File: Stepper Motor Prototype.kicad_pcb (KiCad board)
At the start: 2 copper layers, 142 x 61 mm, 64 parts, among them J1 USB_B_Micro, J2 Screw_Terminal_01x02, J3 Screw_Terminal_01x04, Q1 STD20NF06L, Q2 STD20NF06L, Q3 STD20NF06L, Q4 STD20NF06L, Q5 STD20NF06L, Q6 STD20NF06L, Q7 STD20NF06L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

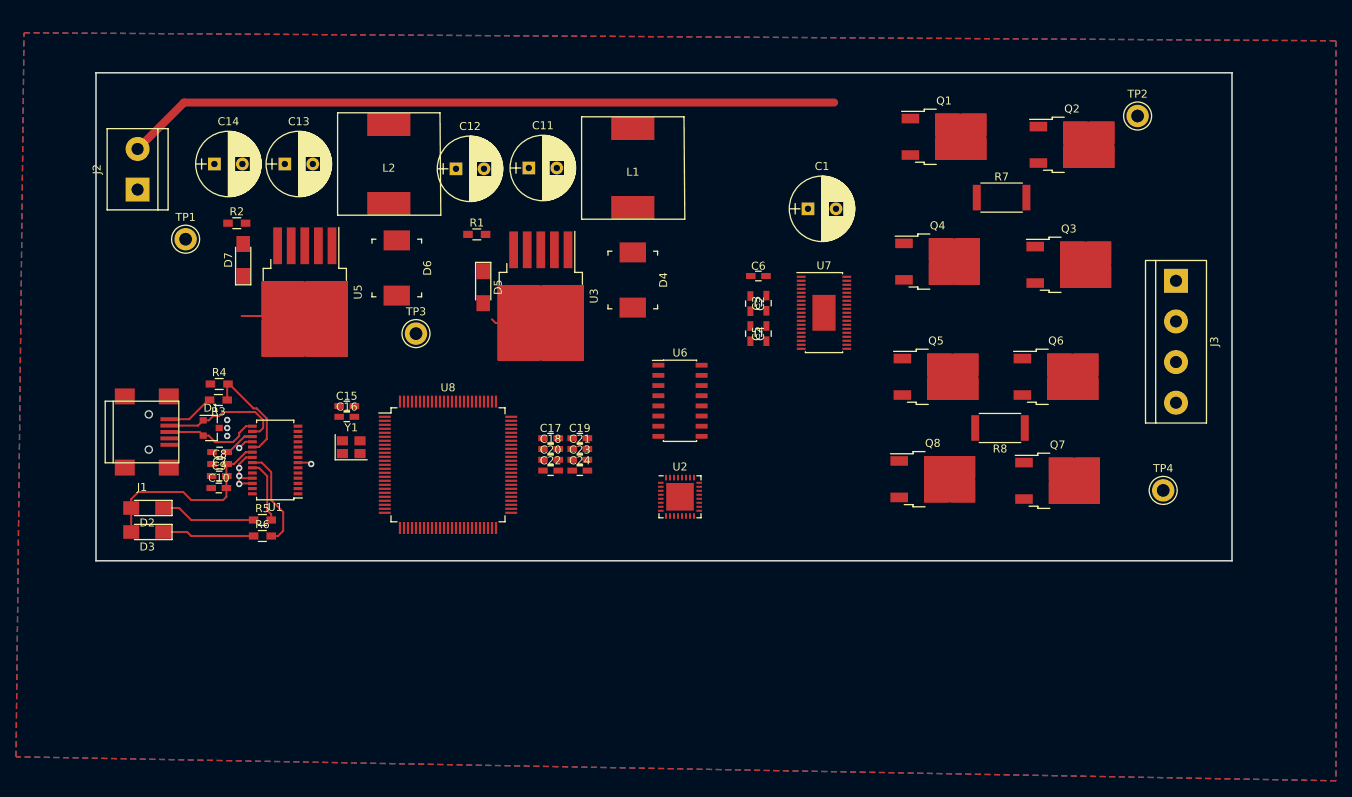
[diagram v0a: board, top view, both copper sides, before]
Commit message: added logic level shifters
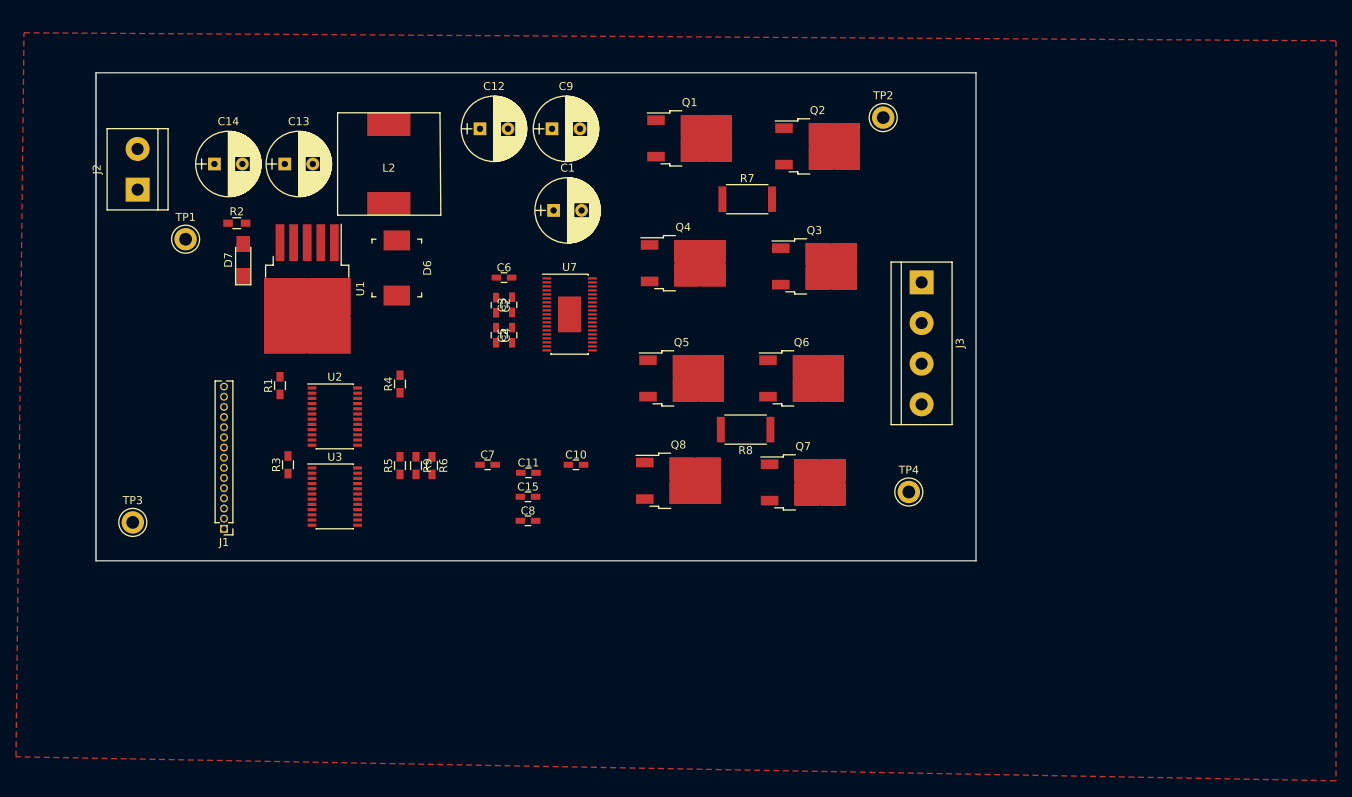
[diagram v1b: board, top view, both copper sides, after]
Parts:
- removed C16: C, Capacitors_SMD:C_0603_HandSoldering
- removed C17, C18, C19, C20, C21, C22, C23, C24: 0.1uF, Capacitors_SMD:C_0603_HandSoldering
- removed D1: SP0502BAHT, TO_SOT_Packages_SMD:SOT-23
- removed D2: TX_LED, LEDs:LED_1206_HandSoldering
- removed D3: RX_LED, LEDs:LED_1206_HandSoldering
- removed D4: D_Schottky, digikey-footprints:DO-214AB
- removed D5: LED, LEDs:LED_1206_HandSoldering
- removed L1: 100uH, my_inductors:Wurth_SMD_Inductor_7447709101
- removed U5: LM2595SX-5.0_NOPB, TO_SOT_Packages_SMD:TO-263-5_TabPin3
- removed U6: S25FL512SAGMFIG11, Housings_SOIC:SOIC-16_3.9x9.9mm_Pitch1.27mm
- removed U8: STM32F407VGTx, Housings_QFP:LQFP-100_14x14mm_Pitch0.5mm
- removed Y1: Crystal_GND24, Crystals:Crystal_SMD_SeikoEpson_TSX3225-4pin_3.2x2.5mm
- added R9: 10k, Resistors_SMD:R_0603_HandSoldering, F.Cu at (110.0, 106.1)
- C10: value 4.7uF -> 0.1uF
- C11: value 120uF -> 0.1uF; footprint Capacitors_THT:CP_Radial_D8.0mm_P3.50mm -> Capacitors_SMD:C_0603_HandSoldering
- C12: value 150uF -> 100uF
- C15: value C -> 1uF
- C9: value 0.1uF -> 100uF; footprint Capacitors_SMD:C_0603_HandSoldering -> Capacitors_THT:CP_Radial_D8.0mm_P3.50mm
- J1: value USB_B_Micro -> Conn_01x15; footprint Connectors:USB_Mini-B -> Pin_Headers:Pin_Header_Straight_1x15_Pitch1.27mm
- R1, R5, R6: value 330R -> 10k
- R3: value 4k7 -> 10k
- U1: value FT232RL -> LM2595SX-5.0_NOPB; footprint Housings_SSOP:TSSOP-28_4.4x9.7mm_Pitch0.65mm -> TO_SOT_Packages_SMD:TO-263-5_TabPin3
- U2: value ESP8266EX -> SN74AXC8T245; footprint Housings_DFN_QFN:QFN-32-1EP_5x5mm_Pitch0.5mm -> Housings_SSOP:TSSOP-24_4.4x7.8mm_Pitch0.65mm
- U3: value LM2595SX-3.3_NOPB -> SN74AXC8T245; footprint TO_SOT_Packages_SMD:TO-263-5_TabPin3 -> Housings_SSOP:TSSOP-24_4.4x7.8mm_Pitch0.65mm
- moved C9 60.1 mm to (127.0, 64.0)
- moved C10 44.7 mm to (130.0, 106.0)
- moved U2 44.3 mm to (99.8, 100.0)
- moved TP3 42.5 mm to (74.6, 113.2)
- moved C8 39.2 mm to (124.0, 113.0)
- moved C11 38.1 mm to (124.0, 107.0)
- moved U3 35.9 mm to (99.8, 110.0), turned to 0 degrees
- moved C7 33.5 mm to (119.0, 106.0), turned to 0 degrees
- moved C2 31.8 mm to (120.0, 86.0)
- moved C3 31.8 mm to (122.0, 86.0)
- moved C4 31.8 mm to (120.0, 89.8)
- moved C5 31.8 mm to (122.0, 89.8)
- moved C6 31.8 mm to (121.0, 82.6)
- moved J3 31.8 mm to (173.2, 83.2)
- moved Q1 31.8 mm to (144.2, 65.2)
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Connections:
- C10 pad 2: +5V -> +1V8
- C11 pad 2: +24V -> +1V8
- C12 pad 1: GND -> +24V
- C12 pad 2: +3V3 -> GND
- C7 pad 1: Net-(C7-Pad1) -> GND
- C7 pad 2: GND -> +3V3
- C8 pad 2: +5V -> +3V3
- C9 pad 1: GND -> +24V
- C9 pad 2: +5V -> GND
- J1 pad 1: Net-(J1-Pad1) -> GND
- J1 pad 2: Net-(D1-Pad1) -> +5V
- J1 pad 3: Net-(D1-Pad2) -> Net-(J1-Pad3)
- J1 pad 4: (no net) -> Net-(J1-Pad4)
- J1 pad 5: GND -> Net-(J1-Pad5)
- J1 pad 6: GND -> Net-(J1-Pad6)
- R1 pad 1: Net-(D5-Pad2) -> Net-(R1-Pad1)
- R3 pad 2: Net-(J1-Pad1) -> +3V3
- R4 pad 1: GND -> Net-(R4-Pad1)
- R4 pad 2: Net-(R3-Pad1) -> +3V3
- R5 pad 1: Net-(D2-Pad1) -> Net-(R5-Pad1)
- R5 pad 2: Net-(R5-Pad2) -> +3V3
- R6 pad 1: Net-(D3-Pad1) -> +1V8
- U1 pad 1: (no net) -> Net-(D6-Pad1)
- U1 pad 2: (no net) -> +24V
- U1 pad 3: (no net) -> GND
- U1 pad 4: Net-(C7-Pad1) -> +5V
- U1 pad 5: (no net) -> GND
- U2 pad 1: (no net) -> +3V3
- U2 pad 11: (no net) -> GND
- U2 pad 12: (no net) -> GND
- U2 pad 13: (no net) -> GND
- U2 pad 16: (no net) -> Net-(U2-Pad16)
- U2 pad 17: (no net) -> Net-(U2-Pad17)
- U2 pad 18: (no net) -> Net-(U2-Pad18)
- U2 pad 19: (no net) -> Net-(U2-Pad19)
- U2 pad 2: (no net) -> Net-(R1-Pad1)
- U2 pad 20: (no net) -> Net-(U2-Pad20)
- U2 pad 21: (no net) -> Net-(U2-Pad21)
- U2 pad 22: (no net) -> Net-(R4-Pad1)
- U2 pad 23: (no net) -> +1V8
- U2 pad 24: (no net) -> +1V8
- U2 pad 3: (no net) -> Net-(J1-Pad15)
- U2 pad 4: (no net) -> Net-(J1-Pad14)
- U2 pad 5: (no net) -> Net-(J1-Pad13)
- U2 pad 6: (no net) -> Net-(J1-Pad12)
- U2 pad 7: (no net) -> Net-(J1-Pad11)
- U2 pad 8: (no net) -> Net-(J1-Pad10)
- U3 pad 1: Net-(D4-Pad1) -> +3V3
- U3 pad 2: +24V -> Net-(R3-Pad1)
- U3 pad 3: GND -> Net-(J1-Pad9)
- U3 pad 4: +3V3 -> Net-(J1-Pad8)
- U3 pad 5: GND -> Net-(J1-Pad7)
- U7 pad 10: (no net) -> Net-(U2-Pad19)
- U7 pad 11: (no net) -> Net-(U2-Pad18)
- U7 pad 12: (no net) -> Net-(U2-Pad17)
- U7 pad 13: (no net) -> Net-(U2-Pad16)
- U7 pad 14: (no net) -> Net-(U3-Pad21)
- U7 pad 15: (no net) -> Net-(U3-Pad20)
- U7 pad 16: (no net) -> Net-(U3-Pad19)
- U7 pad 17: (no net) -> Net-(U3-Pad18)
- U7 pad 18: (no net) -> Net-(R9-Pad2)
- U7 pad 19: (no net) -> Net-(R6-Pad2)
- U7 pad 20: (no net) -> Net-(C15-Pad1)
- U7 pad 8: (no net) -> Net-(U2-Pad21)
- U7 pad 9: (no net) -> Net-(U2-Pad20)
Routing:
- net +24V: track 89.5 -> 0.00 mm
- net GND: track 29.8 -> 0.00 mm, vias 8 -> 0
- net +5V: track 24.9 -> 0.00 mm
- net Net-(D1-Pad1): track 15.3 -> 0.00 mm
- net Net-(R3-Pad1): track 13.5 -> 0.00 mm
- net Net-(R6-Pad2): track 12.6 -> 0.00 mm
- net Net-(D2-Pad1): track 11.9 -> 0.00 mm
- net Net-(D1-Pad2): track 11.9 -> 0.00 mm
- net Net-(D3-Pad1): track 11.5 -> 0.00 mm
- net Net-(R5-Pad2): track 7.98 -> 0.00 mm
- net Net-(J1-Pad1): track 5.99 -> 0.00 mm
- net Net-(C7-Pad1): track 4.35 -> 0.00 mm
- removed copper zone on B.Cu, net GND
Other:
- board size 142 x 61 mm -> 110 x 61 mm

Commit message: removed power supply, basic layout of 1 motor winding complete
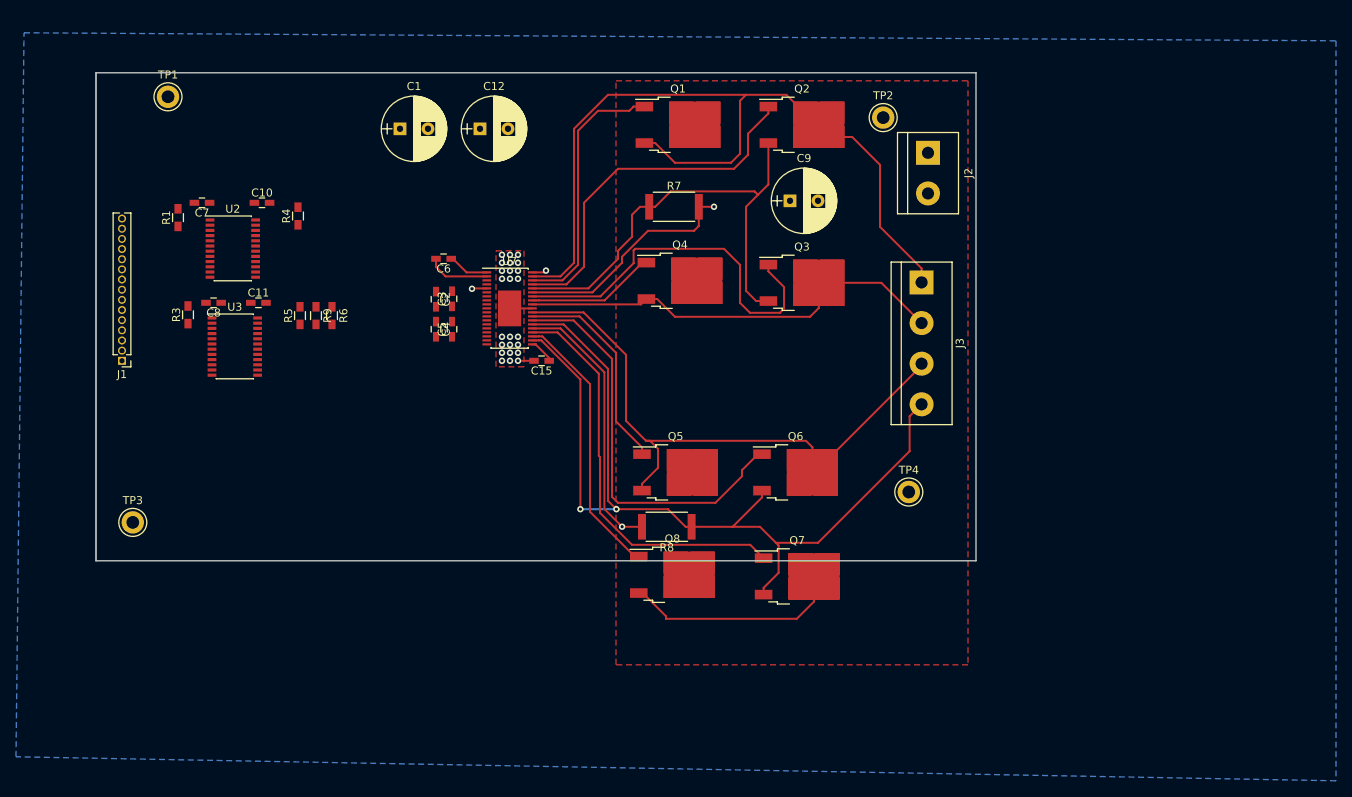
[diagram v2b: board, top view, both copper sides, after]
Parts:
- removed C13: 120uF, Capacitors_THT:CP_Radial_D8.0mm_P3.50mm
- removed C14: 150uF, Capacitors_THT:CP_Radial_D8.0mm_P3.50mm
- removed D6: D_Schottky, digikey-footprints:DO-214AB
- removed D7: LED, LEDs:LED_1206_HandSoldering
- removed L2: L, my_inductors:Wurth_SMD_Inductor_7447709101
- removed R2: 330R, Resistors_SMD:R_0603_HandSoldering
- removed U1: LM2595SX-5.0_NOPB, TO_SOT_Packages_SMD:TO-263-5_TabPin3
- J1: value Conn_01x15 -> Conn_01x16
- moved J2 98.9 mm to (174.0, 67.0), turned to 270 degrees
- moved C10 51.1 mm to (90.8, 73.2)
- moved C7 48.4 mm to (83.2, 73.2), turned to 180 degrees
- moved C8 47.8 mm to (84.7, 85.8), turned to 180 degrees
- moved C11 39.9 mm to (90.3, 85.8)
- moved C9 31.1 mm to (156.8, 73.0)
- moved J1 24.6 mm to (73.2, 93.0)
- moved R1 24.6 mm to (80.2, 75.1)
- moved R4 24.6 mm to (95.2, 74.9)
- moved U2 24.6 mm to (87.1, 79.0)
- moved R3 22.5 mm to (81.5, 87.2)
- moved R5 22.5 mm to (95.5, 87.3)
- moved R6 22.5 mm to (99.5, 87.3)
- moved R9 22.5 mm to (97.5, 87.3)
- moved U3 22.5 mm to (87.3, 91.2)
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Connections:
- net Net-(J3-Pad1) renamed /AOUT1
- net Net-(J3-Pad2) renamed /AOUT2
- net Net-(Q1-Pad1) renamed /A1HS
- net Net-(Q2-Pad1) renamed /A1LS
- net Net-(Q2-Pad3) renamed /A1SENP
- net Net-(Q3-Pad1) renamed /A2LS
- net Net-(Q4-Pad1) renamed /A2HS
- J1 pad 2: +5V -> +1V8
- J1 pad 3: Net-(J1-Pad3) -> +3V3
- U2 pad 3: Net-(J1-Pad15) -> (no net)
- U2 pad 4: Net-(J1-Pad14) -> Net-(J1-Pad15)
- U2 pad 5: Net-(J1-Pad13) -> Net-(J1-Pad14)
- U2 pad 6: Net-(J1-Pad12) -> Net-(J1-Pad13)
- U2 pad 7: Net-(J1-Pad11) -> Net-(J1-Pad12)
- U2 pad 8: Net-(J1-Pad10) -> Net-(J1-Pad11)
- U3 pad 3: Net-(J1-Pad9) -> Net-(J1-Pad10)
- U3 pad 4: Net-(J1-Pad8) -> Net-(J1-Pad9)
- U3 pad 5: Net-(J1-Pad7) -> Net-(J1-Pad8)
- U3 pad 6: Net-(J1-Pad6) -> Net-(J1-Pad7)
- U3 pad 7: Net-(J1-Pad5) -> Net-(J1-Pad6)
- U3 pad 8: Net-(J1-Pad4) -> Net-(J1-Pad5)
- U3 pad 9: Net-(J1-Pad3) -> Net-(J1-Pad4)
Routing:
- net Net-(J3-Pad4): track 0.00 -> 121.5 mm, vias 0 -> 2
- net /AOUT1: track 0.00 -> 102.0 mm
- net Net-(J3-Pad3): track 0.00 -> 79.7 mm
- net GND: track 0.00 -> 71.5 mm, vias 0 -> 28
- net /A1SENP: track 0.00 -> 58.6 mm
- net /AOUT2: track 0.00 -> 54.8 mm
- net Net-(Q6-Pad1): track 0.00 -> 51.2 mm
- net Net-(Q7-Pad1): track 0.00 -> 50.6 mm
- net /A2LS: track 0.00 -> 47.5 mm
- net /A1LS: track 0.00 -> 45.4 mm
- net Net-(Q8-Pad1): track 0.00 -> 34.1 mm
- net /A1HS: track 0.00 -> 32.8 mm
- net Net-(Q7-Pad2): track 0.00 -> 27.5 mm
- net Net-(Q5-Pad1): track 0.00 -> 26.4 mm
- net /A2HS: track 0.00 -> 16.2 mm
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- added copper zone on F.Cu, net +24V
- added copper zone on In2.Cu, net +24V
- added copper zone on B.Cu, net GND
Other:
- copper layers 2 -> 4

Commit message: continued working on motor power section.  Still need to layout mirrored side.
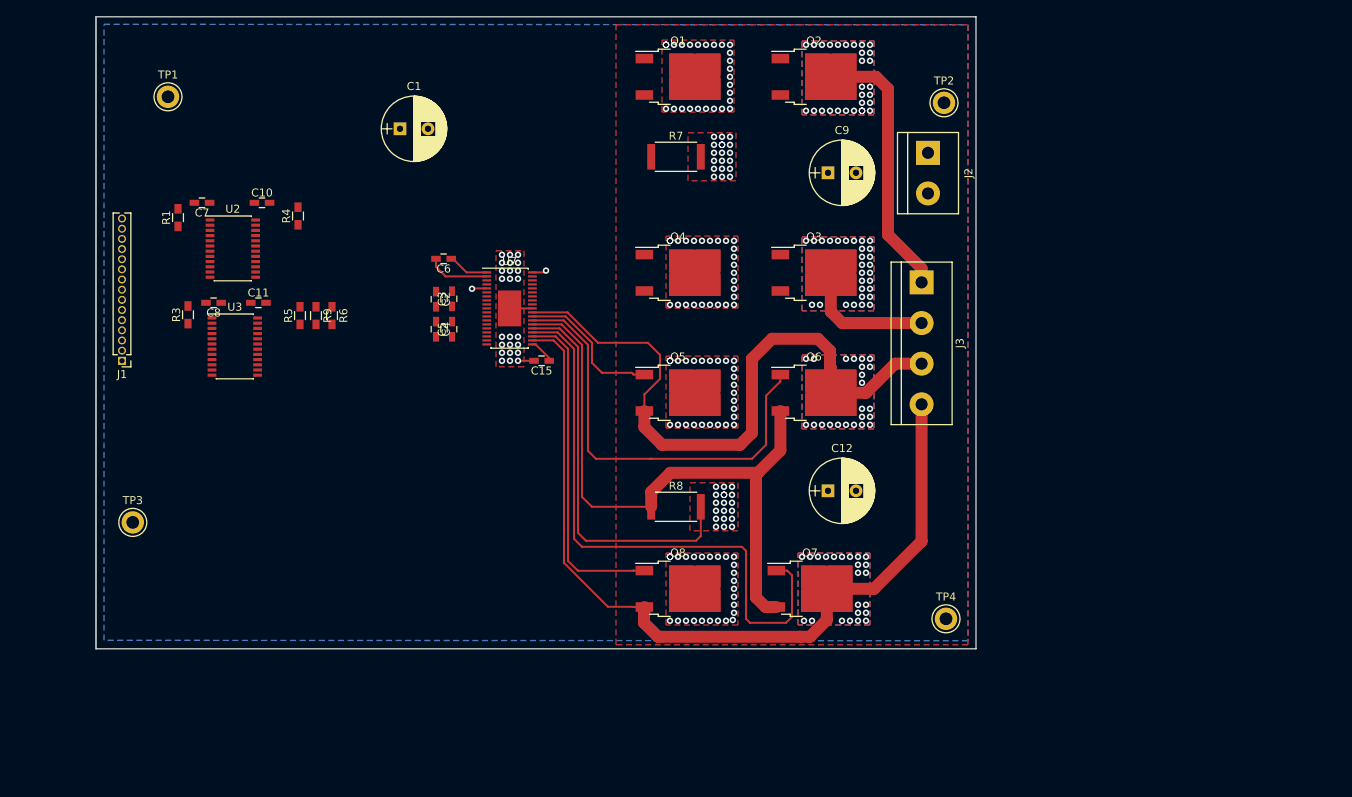
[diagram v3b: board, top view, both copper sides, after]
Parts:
- moved C12 62.8 mm to (161.5, 109.2)
- moved TP4 16.5 mm to (176.2, 125.2)
- moved Q6 10.2 mm to (159.8, 97.0)
- moved Q5 9.95 mm to (142.8, 97.0)
- moved TP2 7.82 mm to (176.0, 60.8)
- moved R7 6.25 mm to (142.5, 67.5)
- moved Q2 6.18 mm to (159.8, 57.5)
- moved Q1 6.00 mm to (142.8, 57.5)
- moved C9 5.90 mm to (161.5, 69.5)
- moved R8 2.75 mm to (142.5, 111.2), turned to 0 degrees
- moved Q7 2.23 mm to (159.2, 121.5)
- moved Q3 1.95 mm to (159.8, 82.0)
- moved Q8 1.88 mm to (142.8, 121.5)
- moved Q4 1.03 mm to (142.8, 82.0)
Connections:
- Q6 pad 3: Net-(J3-Pad4) -> Net-(Q6-Pad3)
- Q7 pad 2: Net-(Q7-Pad2) -> Net-(J3-Pad4)
- Q7 pad 3: Net-(J3-Pad4) -> Net-(Q6-Pad3)
- Q8 pad 3: Net-(Q7-Pad2) -> Net-(J3-Pad4)
- R8 pad 1: Net-(J3-Pad4) -> Net-(Q6-Pad3)
- U7 pad 25: Net-(J3-Pad4) -> Net-(Q6-Pad3)
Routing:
- net Net-(Q6-Pad3): track 0.00 -> 79.1 mm
- net /AOUT1: track 102.0 -> 33.7 mm, vias 0 -> 30
- net /A1SENP: track 58.6 -> 0.00 mm
- net /A2LS: track 47.5 -> 0.00 mm
- net /A1LS: track 45.4 -> 0.00 mm
- net /AOUT2: track 54.8 -> 16.8 mm, vias 0 -> 29
- net /A1HS: track 32.8 -> 0.00 mm
- net Net-(Q7-Pad2): track 27.5 -> 0.00 mm
- net Net-(Q7-Pad1): track 50.6 -> 74.1 mm
- net Net-(J3-Pad4): track 121.5 -> 105.1 mm, vias 2 -> 23
- net /A2HS: track 16.2 -> 0.00 mm
- net GND: track 71.5 -> 58.1 mm, vias 28 -> 66
- net Net-(Q5-Pad1): track 26.4 -> 18.5 mm
- net Net-(Q8-Pad1): track 34.1 -> 41.7 mm
- net Net-(J3-Pad3): track 79.7 -> 83.8 mm, vias 0 -> 23
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- added copper zone on B.Cu, net /AOUT1
- added copper zone on F.Cu, net /AOUT1
- added copper zone on B.Cu, net /AOUT2
- added copper zone on F.Cu, net /AOUT2
- added copper zone on B.Cu, net Net-(J3-Pad3)
- added copper zone on F.Cu, net Net-(J3-Pad3)
- added copper zone on B.Cu, net Net-(J3-Pad4)
- added copper zone on F.Cu, net Net-(J3-Pad4)
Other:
- board size 110 x 61 mm -> 110 x 79 mm
- rule pad_to_mask_clearance: 0.2 -> 0

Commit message: finished laying out second side of motor power section
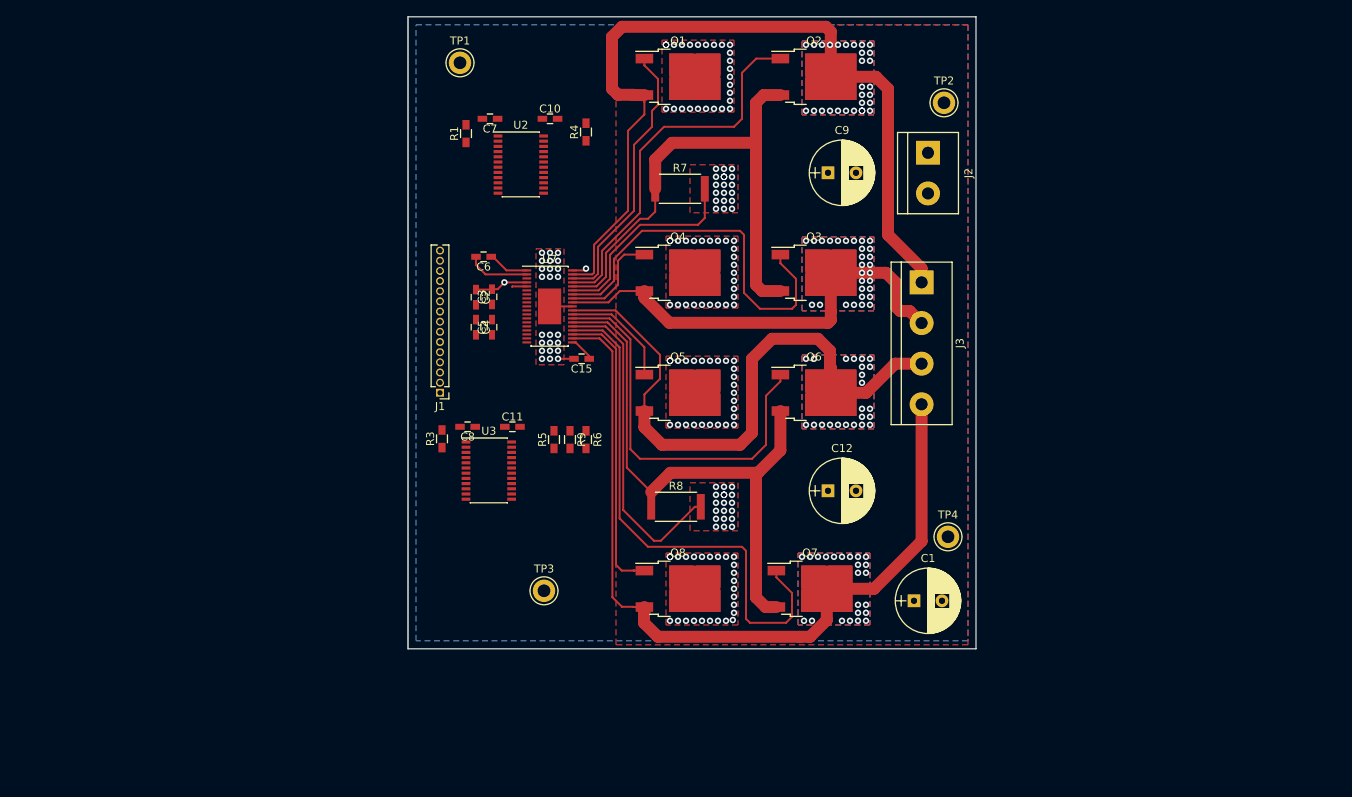
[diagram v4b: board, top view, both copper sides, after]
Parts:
- moved C1 87.2 mm to (172.2, 123.0)
- moved TP3 52.1 mm to (126.0, 121.8)
- moved J1 40.0 mm to (113.0, 97.0)
- moved C10 37.5 mm to (126.8, 62.8)
- moved C7 37.5 mm to (119.2, 62.8)
- moved R1 37.5 mm to (116.2, 64.6)
- moved R4 37.5 mm to (131.2, 64.4)
- moved U2 37.5 mm to (123.1, 68.5)
- moved TP1 36.7 mm to (115.5, 55.8)
- moved C11 35.3 mm to (122.0, 101.2)
- moved C8 35.3 mm to (116.5, 101.2)
- moved R3 35.3 mm to (113.2, 102.8)
- moved R5 35.3 mm to (127.2, 102.8)
- moved R6 35.3 mm to (131.2, 102.8)
- moved R9 35.3 mm to (129.2, 102.8)
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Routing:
- net /AOUT1: track 33.7 -> 105.9 mm
- net /A1SENP: track 0.00 -> 65.5 mm
- net /A2LS: track 0.00 -> 48.4 mm
- net /A1LS: track 0.00 -> 47.3 mm
- net /AOUT2: track 16.8 -> 56.8 mm
- net /A1HS: track 0.00 -> 34.4 mm
- net GND: track 58.1 -> 75.3 mm, vias 66 -> 65
- net /A2HS: track 0.00 -> 13.0 mm
- net Net-(Q6-Pad3): track 79.1 -> 71.6 mm
- net Net-(Q7-Pad1): track 74.1 -> 67.0 mm
- net +24V: track 0.00 -> 6.72 mm, vias 108 -> 109
- net Net-(J3-Pad3): track 83.8 -> 78.9 mm
- net Net-(Q6-Pad1): track 54.6 -> 49.8 mm
- net Net-(Q8-Pad1): track 41.7 -> 37.1 mm
- net Net-(Q5-Pad1): track 18.5 -> 14.1 mm
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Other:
- board size 110 x 79 mm -> 71 x 79 mm
